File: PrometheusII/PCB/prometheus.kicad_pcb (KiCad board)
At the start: 4 copper layers, 223.5 x 222.3 mm, 203 parts, among them J1 0878311420, J10 Conn_02x02_Odd_Even, J11 Conn_02x02_Odd_Even, J16 Conn_02x07_Odd_Even, J17 Conn_02x07_Odd_Even, J18 Conn_02x07_Odd_Even, J19 Conn_02x07_Odd_Even, J2 Conn_02x08_Odd_Even, J3 Conn_02x02_Odd_Even, J4 Conn_02x02_Odd_Even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

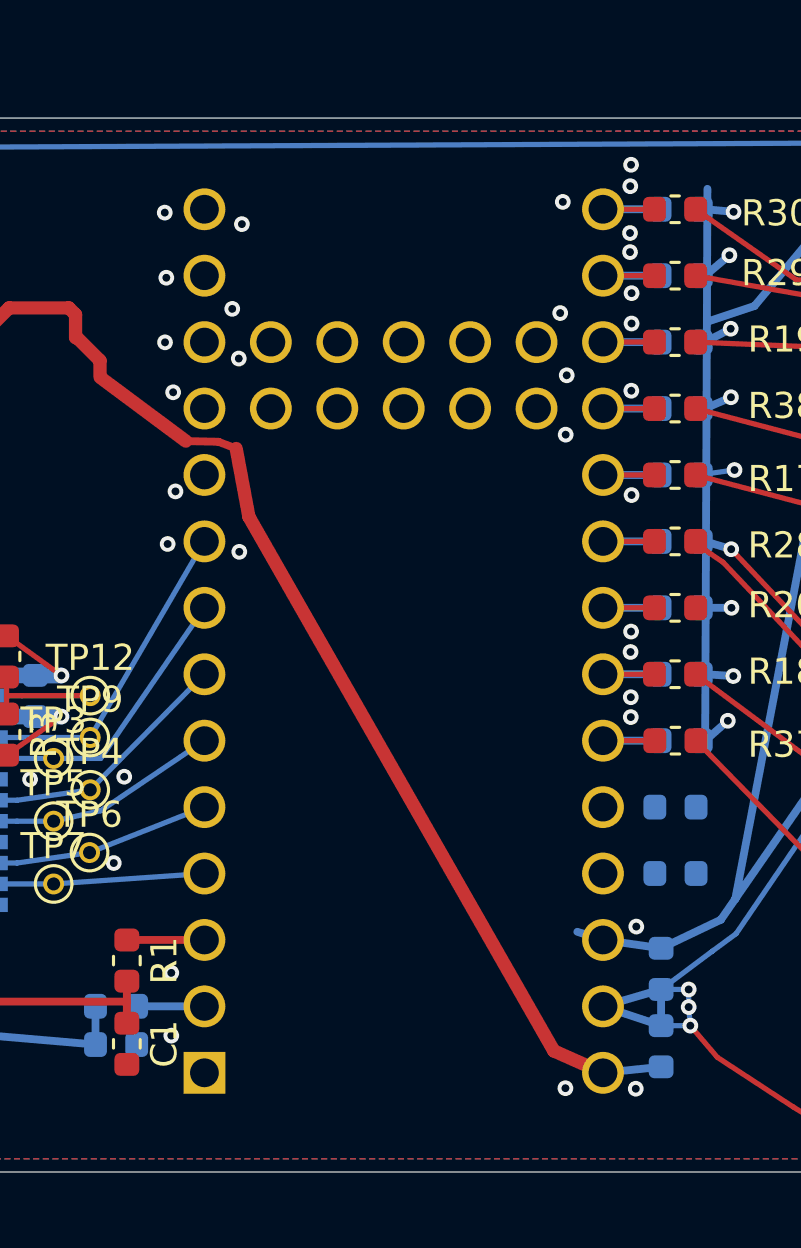
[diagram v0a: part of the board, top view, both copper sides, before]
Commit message: CPLD power supply routing
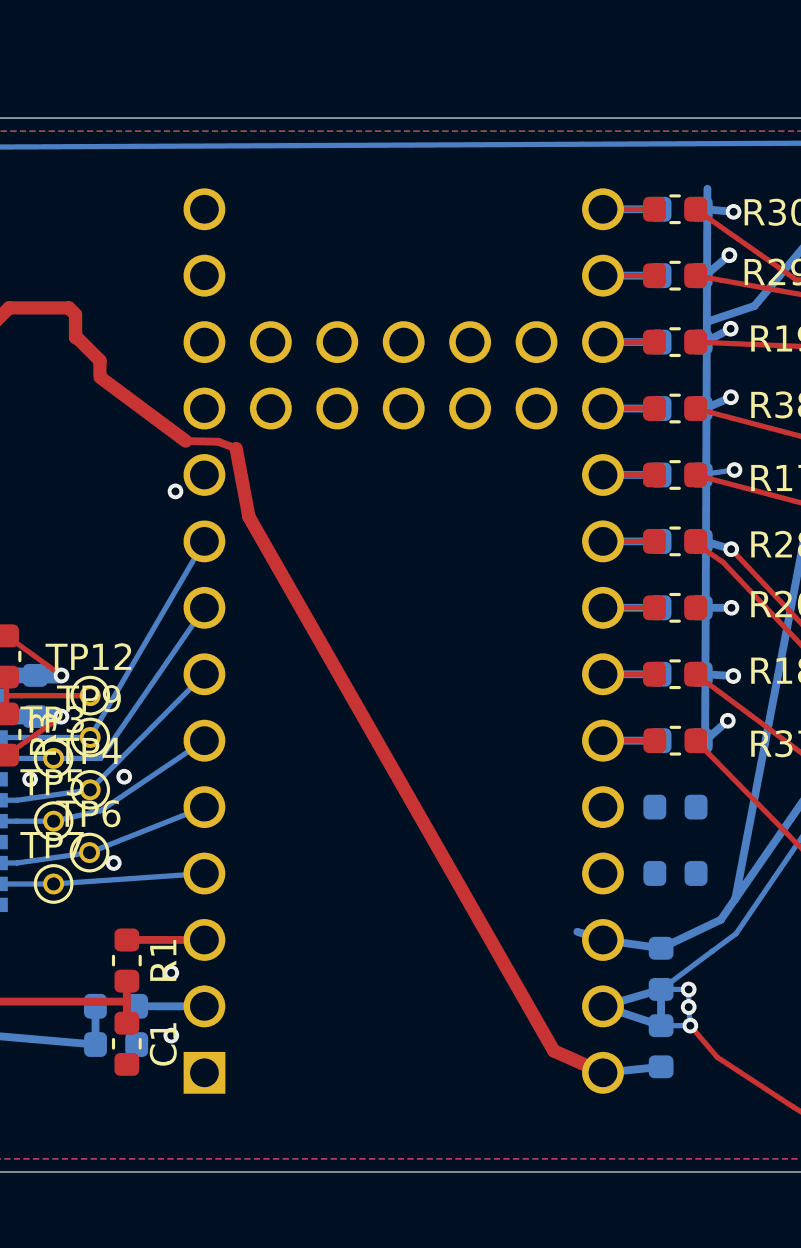
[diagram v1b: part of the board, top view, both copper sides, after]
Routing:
- net +3V3: track 619.6 -> 662.6 mm
- net GND: vias 107 -> 79
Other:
- net class Default: clearance 0.15 -> 0.16; trace_width 0.1524 -> 0.16
- rule trace_clearance: 0.15 -> 0.16
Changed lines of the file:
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@@
     (thickness 1.6)
     (drawings 86)
-    (tracks 1112)
+    (tracks 1089)
     (zones 0)
     (modules 203)
@@
   )
   (setup
-    (last_trace_width 0.2)
+    (last_trace_width 0.6)
     (user_trace_width 0.15)
     (user_trace_width 0.1524)
@@
     (user_trace_width 0.508)
     (user_trace_width 0.6)
-    (trace_clearance 0.15)
+    (trace_clearance 0.16)
     (zone_clearance 0.2)
     (zone_45_only no)
@@
   (net 162 "Net-(C49-Pad2)")
   (net_class Default "This is the default net class."
-    (clearance 0.15)
-    (trace_width 0.1524)
+    (clearance 0.16)
+    (trace_width 0.16)
     (via_dia 0.6)
     (via_drill 0.3)
@@
   (segment (start 134.95 115.5435) (end 134.924673 113.137173) (width 0.3) (layer B.Cu) (net 1))
   (segment (start 134.924673 113.137173) (end 132.1535 113.406) (width 0.3) (layer B.Cu) (net 1))
-  (via (at 181.6935 92.686) (size 0.6) (drill 0.3) (layers F.Cu B.Cu) (net 1))
-  (via (at 181.7535 95.176) (size 0.6) (drill 0.3) (layers F.Cu B.Cu) (net 1))
-  (via (at 181.7035 97.646) (size 0.6) (drill 0.3) (layers F.Cu B.Cu) (net 1))
-  (via (at 182.0135 99.556) (size 0.6) (drill 0.3) (layers F.Cu B.Cu) (net 1))
-  (via (at 184.5435 105.656) (size 0.6) (drill 0.3) (layers F.Cu B.Cu) (net 1))
-  (via (at 196.8135 96.526) (size 0.6) (drill 0.3) (layers F.Cu B.Cu) (net 1))
-  (via (at 197.0235 101.176) (size 0.6) (drill 0.3) (layers F.Cu B.Cu) (net 1))
-  (via (at 196.9135 92.276) (size 0.6) (drill 0.3) (layers F.Cu B.Cu) (net 1))
-  (via (at 199.5235 90.856) (size 0.6) (drill 0.3) (layers F.Cu B.Cu) (net 1))
-  (via (at 199.4935 91.676) (size 0.6) (drill 0.3) (layers F.Cu B.Cu) (net 1))
-  (via (at 199.4835 93.466) (size 0.6) (drill 0.3) (layers F.Cu B.Cu) (net 1))
-  (via (at 199.4835 94.196) (size 0.6) (drill 0.3) (layers F.Cu B.Cu) (net 1))
-  (via (at 199.5235 108.706) (size 0.6) (drill 0.3) (layers F.Cu B.Cu) (net 1))
-  (via (at 199.5035 109.486) (size 0.6) (drill 0.3) (layers F.Cu B.Cu) (net 1))
-  (via (at 199.5135 111.216) (size 0.6) (drill 0.3) (layers F.Cu B.Cu) (net 1))
-  (via (at 199.5135 111.976) (size 0.6) (drill 0.3) (layers F.Cu B.Cu) (net 1))
-  (via (at 199.7235 119.986) (size 0.6) (drill 0.3) (layers F.Cu B.Cu) (net 1))
-  (via (at 199.7035 126.186) (size 0.6) (drill 0.3) (layers F.Cu B.Cu) (net 1))
   (via (at 167.6935 94.166) (size 0.6) (drill 0.3) (layers F.Cu B.Cu) (net 1))
   (segment (start 124.968 102.616) (end 121.8935 103.896) (width 0.2) (layer B.Cu) (net 1))
@@
   (segment (start 165.33467 100.37717) (end 163.8553 100.2284) (width 0.508) (layer B.Cu) (net 1))
   (via (at 165.0335 100.006) (size 0.6) (drill 0.3) (layers F.Cu B.Cu) (net 1))
-  (via (at 181.8035 105.356) (size 0.6) (drill 0.3) (layers F.Cu B.Cu) (net 1))
-  (via (at 197.0635 98.906) (size 0.6) (drill 0.3) (layers F.Cu B.Cu) (net 1))
-  (via (at 184.2735 96.366) (size 0.6) (drill 0.3) (layers F.Cu B.Cu) (net 1))
-  (via (at 184.6435 93.126) (size 0.6) (drill 0.3) (layers F.Cu B.Cu) (net 1))
-  (via (at 197.0135 126.166) (size 0.6) (drill 0.3) (layers F.Cu B.Cu) (net 1))
   (via (at 163.4935 125.406) (size 0.6) (drill 0.3) (layers F.Cu B.Cu) (net 1))
   (segment (start 132.0835 113.336) (end 131.9275 111.999) (width 0.3) (layer B.Cu) (net 1))
@@
   (segment (start 226.2135 122.336) (end 225.8435 121.536) (width 0.3) (layer B.Cu) (net 1))
   (via (at 226.2135 122.336) (size 0.6) (drill 0.3) (layers F.Cu B.Cu) (net 1))
-  (via (at 199.5335 99.496) (size 0.6) (drill 0.3) (layers F.Cu B.Cu) (net 1))
   (segment (start 202.3572 105.2576) (end 203.3535 105.556) (width 0.3) (layer B.Cu) (net 1))
   (via (at 203.3535 105.556) (size 0.6) (drill 0.3) (layers F.Cu B.Cu) (net 1))
-  (via (at 199.5435 103.486) (size 0.6) (drill 0.3) (layers F.Cu B.Cu) (net 1))
   (segment (start 202.3572 97.6376) (end 203.3335 97.126) (width 0.3) (layer B.Cu) (net 1))
   (via (at 203.3335 97.126) (size 0.6) (drill 0.3) (layers F.Cu B.Cu) (net 1))
-  (via (at 199.5435 96.926) (size 0.6) (drill 0.3) (layers F.Cu B.Cu) (net 1))
-  (via (at 199.5435 95.766) (size 0.6) (drill 0.3) (layers F.Cu B.Cu) (net 1))
-  (via (at 184.5235 98.266) (size 0.6) (drill 0.3) (layers F.Cu B.Cu) (net 1))
-  (via (at 182.1035 103.346) (size 0.6) (drill 0.3) (layers F.Cu B.Cu) (net 1))
   (segment (start 48.1035 102.706) (end 46.5835 103.759) (width 0.3) (layer B.Cu) (net 1))
   (segment (start 54.2035 102.456) (end 48.1035 102.706) (width 0.3) (layer B.Cu) (net 1))
@@
   (segment (start 215.6059 108.4372) (end 213.906 110.2487) (width 0.3) (layer B.Cu) (net 6))
   (segment (start 213.906 110.2487) (end 211.8613 110.2487) (width 0.3) (layer B.Cu) (net 6))
-  (segment (start 198.4502 120.4976) (end 183.2355 116.713) (width 0.3) (layer In1.Cu) (net 6))
-  (segment (start 198.4502 120.4976) (end 183.9975 109.0295) (width 0.3) (layer In1.Cu) (net 6))
-  (segment (start 183.9975 109.0295) (end 182.2195 109.0295) (width 0.3) (layer In1.Cu) (net 6))
   (segment (start 137.5663 107.188) (end 136.6035 107.186) (width 0.3) (layer B.Cu) (net 6))
   (segment (start 110.2105 109.2985) (end 109.9725 107.63) (width 0.3) (layer F.Cu) (net 6))
@@
   (segment (start 147.5135 121.026) (end 140.4365 120.904) (width 0.3) (layer In1.Cu) (net 6))
   (segment (start 148.0835 128.156) (end 147.5135 121.026) (width 0.3) (layer In1.Cu) (net 6))
-  (segment (start 182.0925 114.427) (end 183.934 114.173) (width 0.3) (layer In1.Cu) (net 6))
-  (segment (start 183.934 114.173) (end 198.4502 120.4976) (width 0.3) (layer In1.Cu) (net 6))
   (segment (start 101.4535 95.936) (end 102.3535 95.316) (width 0.2) (layer F.Cu) (net 6))
   (segment (start 97.8335 97.276) (end 101.4535 95.936) (width 0.2) (layer F.Cu) (net 6))
@@
   (segment (start 172.4435 120.856) (end 172.4435 122.156) (width 0.3) (layer B.Cu) (net 1))
   (via (at 172.4435 122.156) (size 0.6) (drill 0.3) (layers F.Cu B.Cu) (net 1))
+  (via (at 182.1035 103.346) (size 0.6) (drill 0.3) (layers F.Cu B.Cu) (net 1))
   (segment (start 162.09 99.7585) (end 160.4435 103.156) (width 0.3) (layer In1.Cu) (net 2))
   (segment (start 162.099933 99.757916) (end 162.09 99.7585) (width 0.3) (layer In1.Cu) (net 2))
@@
   (segment (start 167.6435 103.356) (end 167.6485 106.656) (width 0.2) (layer B.Cu) (net 6))
   (segment (start 170.0435 102.681) (end 167.6435 103.356) (width 0.2) (layer B.Cu) (net 6))
+  (segment (start 177.7435 111.956) (end 178.4435 111.956) (width 0.6) (layer In1.Cu) (net 6))
+  (segment (start 178.5435 111.956) (end 179.0435 111.956) (width 0.4) (layer In1.Cu) (net 6))
+  (segment (start 183.5135 111.586) (end 198.4502 120.4976) (width 0.6) (layer In1.Cu) (net 6))
+  (segment (start 179.2435 111.956) (end 183.5135 111.586) (width 0.6) (layer In1.Cu) (net 6))
+  (segment (start 183.6635 109.096) (end 198.4502 120.4976) (width 0.6) (layer In1.Cu) (net 6))
+  (segment (start 167.6485 106.656) (end 168.5435 108.356) (width 0.6) (layer In1.Cu) (net 6))
+  (segment (start 168.5435 108.356) (end 183.6635 109.096) (width 0.6) (layer In1.Cu) (net 6))
+  (segment (start 183.2535 119.226) (end 198.4502 120.4976) (width 0.6) (layer In1.Cu) (net 6))
+  (segment (start 160.7435 116.7385) (end 177.3235 119.486) (width 0.6) (layer In1.Cu) (net 6))
+  (segment (start 177.3235 119.486) (end 183.2535 119.226) (width 0.6) (layer In1.Cu) (net 6))
   (segment (start 158.2435 113.556) (end 158.2435 111.956) (width 0.2) (layer B.Cu) (net 8))
   (segment (start 160.256 109.756) (end 158.5435 109.756) (width 0.2) (layer B.Cu) (net 8))

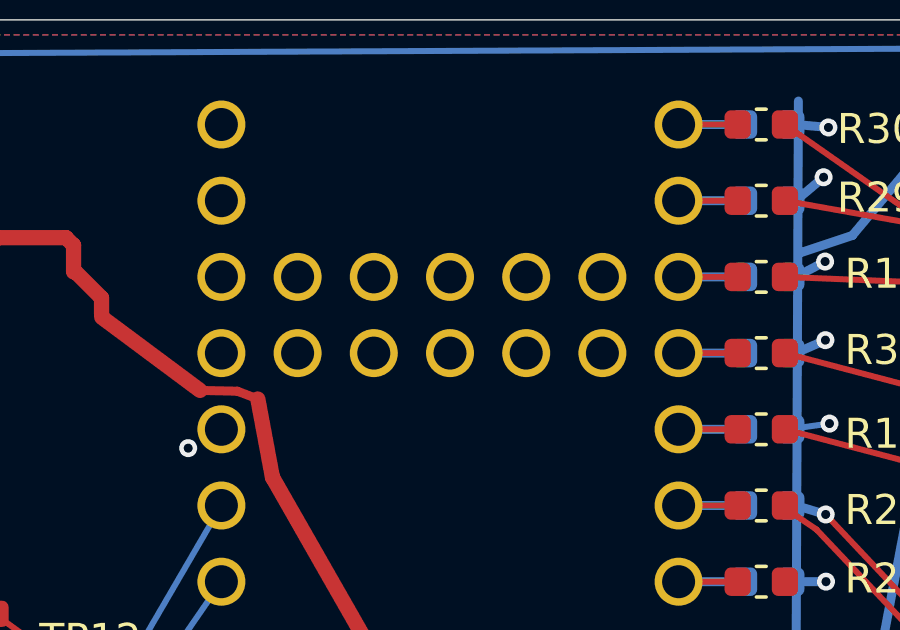
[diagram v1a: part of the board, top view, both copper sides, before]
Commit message: Removed underside pins from teensy
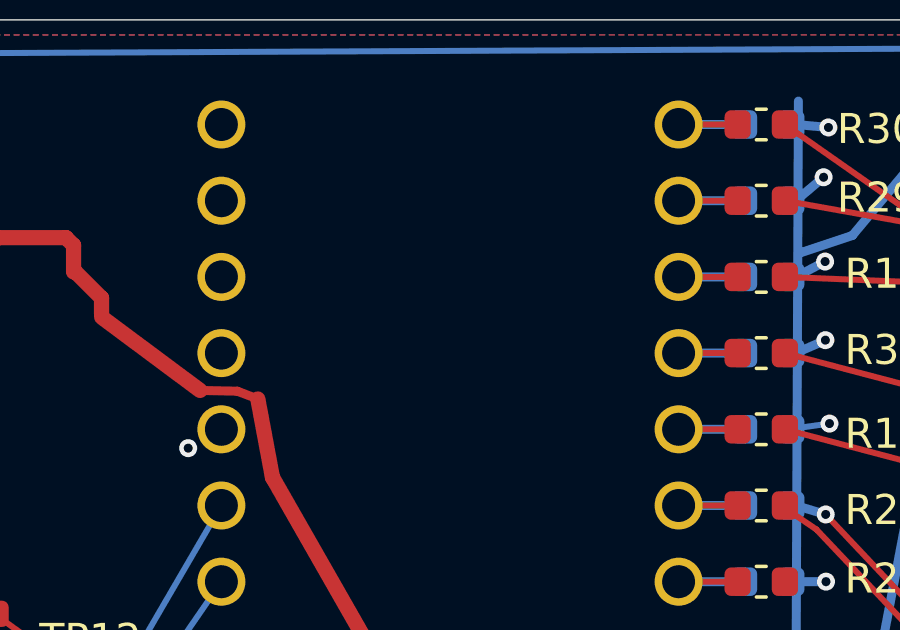
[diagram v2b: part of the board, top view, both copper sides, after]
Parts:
- U1: footprint ttt_lib:Teensy40_underpins -> ttt_lib:Teensy40_outerpins
